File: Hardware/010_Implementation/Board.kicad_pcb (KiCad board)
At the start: 2 copper layers, 87.5 x 70 mm, 70 parts, among them IC1 SN65HVD233-HT, J1 Conn_01x08_Female, J2 JTAG Jumper Pins, J3 DSUB9, K1 G5V-2-DC5, K2 G5V-2-DC5, Q1 BC817, SW1 SW_Push, U1 TPS62160DGK, U2 ESP32-DEVKITC-32D

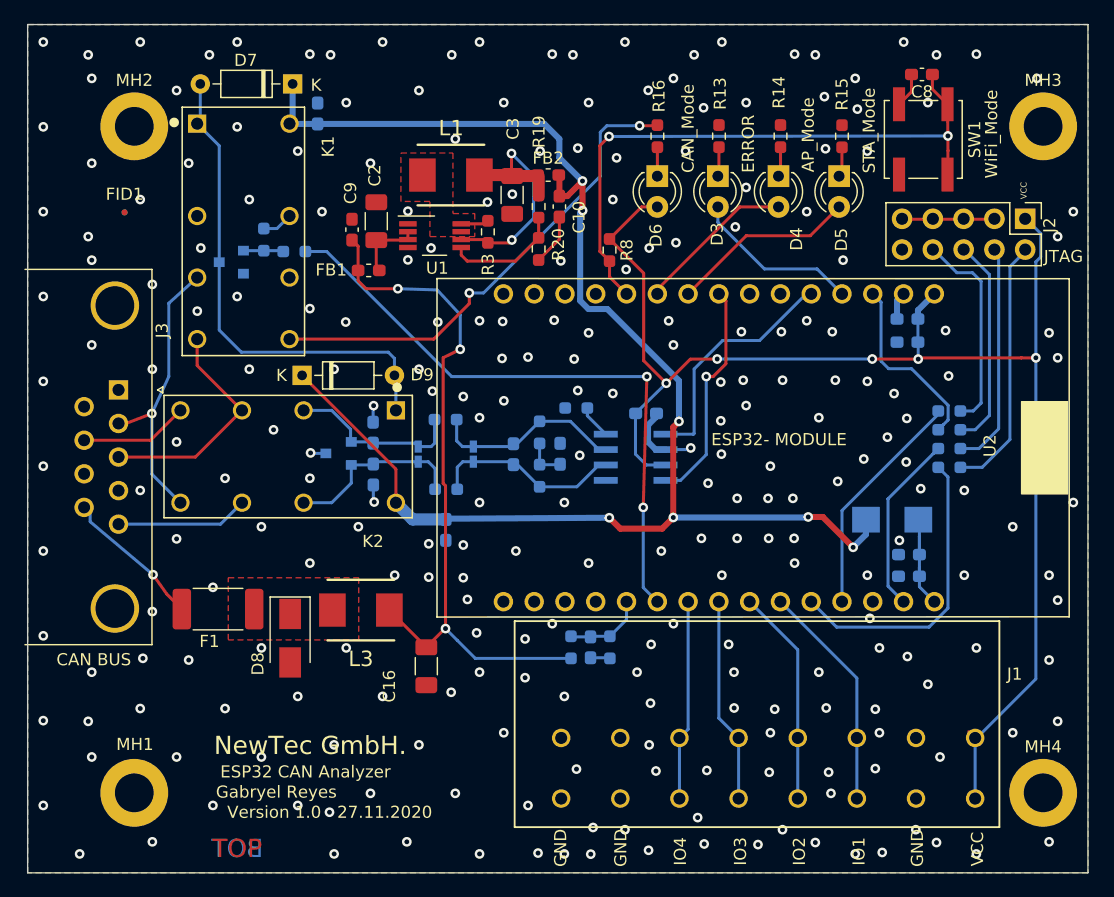
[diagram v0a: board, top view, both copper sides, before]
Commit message: Board Version 1.1 Fixed Relay Supply, standard Pins for CAN Transceiver and added CAN high and Low Labels
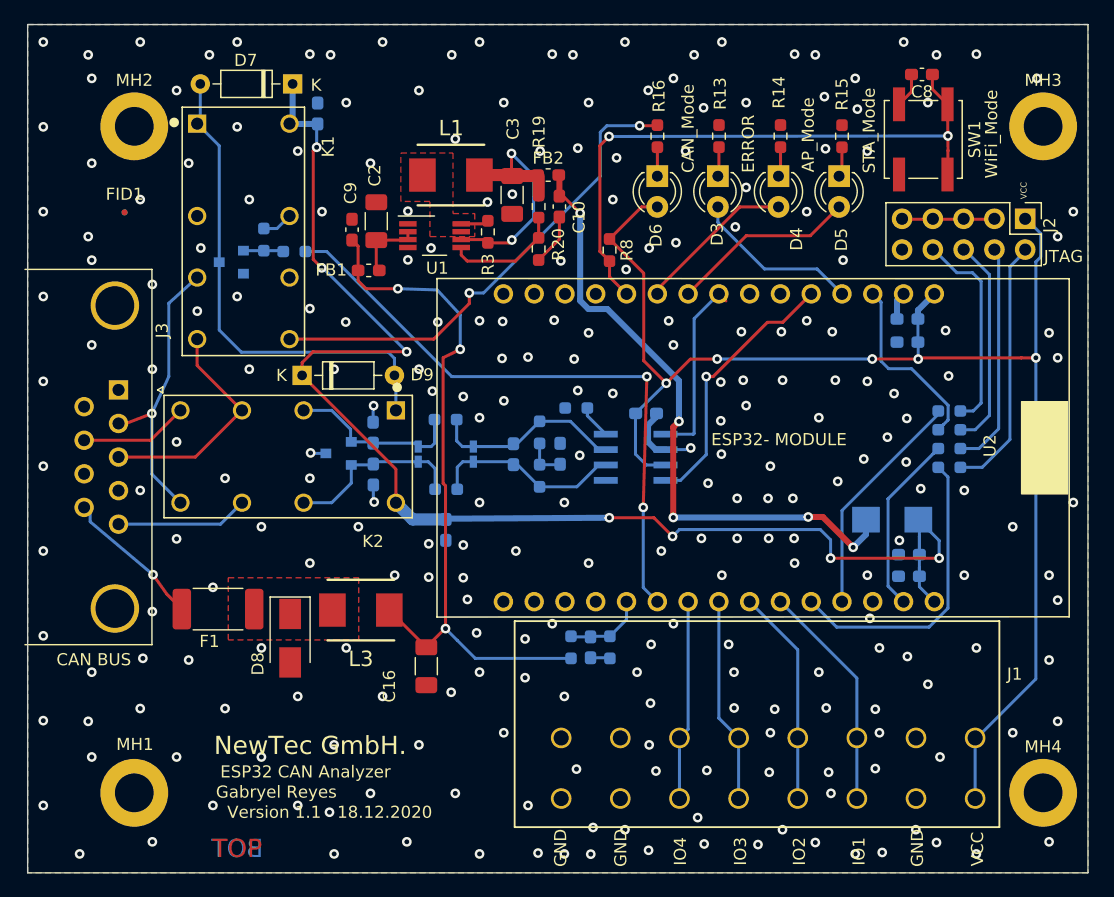
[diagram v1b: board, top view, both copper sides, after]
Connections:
- C11 pad 1: +5V -> /Connector/Relay_Supply
- C12 pad 1: Net-(C12-Pad1) -> /Connector/Relay_Supply
- C13 pad 2: Net-(C12-Pad1) -> /Connector/Relay_Supply
- C18 pad 1: +5V -> /Connector/Relay_Supply
- D2 pad C: Net-(C12-Pad1) -> /Connector/Relay_Supply
- D7 pad 1: +5V -> /Connector/Relay_Supply
- D9 pad 1: +5V -> /Connector/Relay_Supply
- J2 pad 10: (no net) -> Net-(J2-Pad10)
- J3 pad 0: GND -> (no net)
- J3 pad 1: (no net) -> Net-(J3-Pad1)
- J3 pad 4: (no net) -> Net-(J3-Pad4)
- J3 pad 6: (no net) -> Net-(J3-Pad6)
- J3 pad 8: (no net) -> Net-(J3-Pad8)
- K1 pad 16: +5V -> /Connector/Relay_Supply
- K2 pad 16: +5V -> /Connector/Relay_Supply
- U2 pad 1: (no net) -> Net-(U2-Pad1)
- U2 pad 15: Net-(C12-Pad1) -> /Connector/Relay_Supply
- U2 pad 16: (no net) -> Net-(U2-Pad16)
- U2 pad 17: (no net) -> Net-(U2-Pad17)
- U2 pad 18: (no net) -> Net-(U2-Pad18)
- U2 pad 19: (no net) -> Net-(U2-Pad19)
- U2 pad 2: (no net) -> Net-(U2-Pad2)
- U2 pad 23: /CAN_Transceiver/CAN_Rx -> /CAN_Transceiver/CAN_Tx
- U2 pad 24: (no net) -> Net-(U2-Pad24)
- U2 pad 25: (no net) -> Net-(U2-Pad25)
- U2 pad 26: /CAN_Transceiver/CAN_Tx -> /CAN_Transceiver/CAN_Rx
- U2 pad 3: (no net) -> Net-(U2-Pad3)
- U2 pad 4: (no net) -> Net-(U2-Pad4)
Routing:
- net /Connector/Relay_Supply: track 0.00 -> 113.9 mm, vias 0 -> 7
- net +5V: track 123.9 -> 52.3 mm, vias 7 -> 5
- net Net-(C12-Pad1): track 9.83 -> 0.00 mm
- net /CAN_Transceiver/CAN_Tx: track 19.9 -> 15.6 mm
- net /CAN_Transceiver/CAN_Rx: track 18.8 -> 22.6 mm
- net GND: vias 257 -> 256
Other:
- board text added: "CAN_H"
- board text added: "CAN_L"
- board text added: "Version 1.1 18.12.2020"
- board text removed: "Version 1.0 27.11.2020"
